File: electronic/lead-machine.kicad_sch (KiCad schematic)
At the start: 0 parts

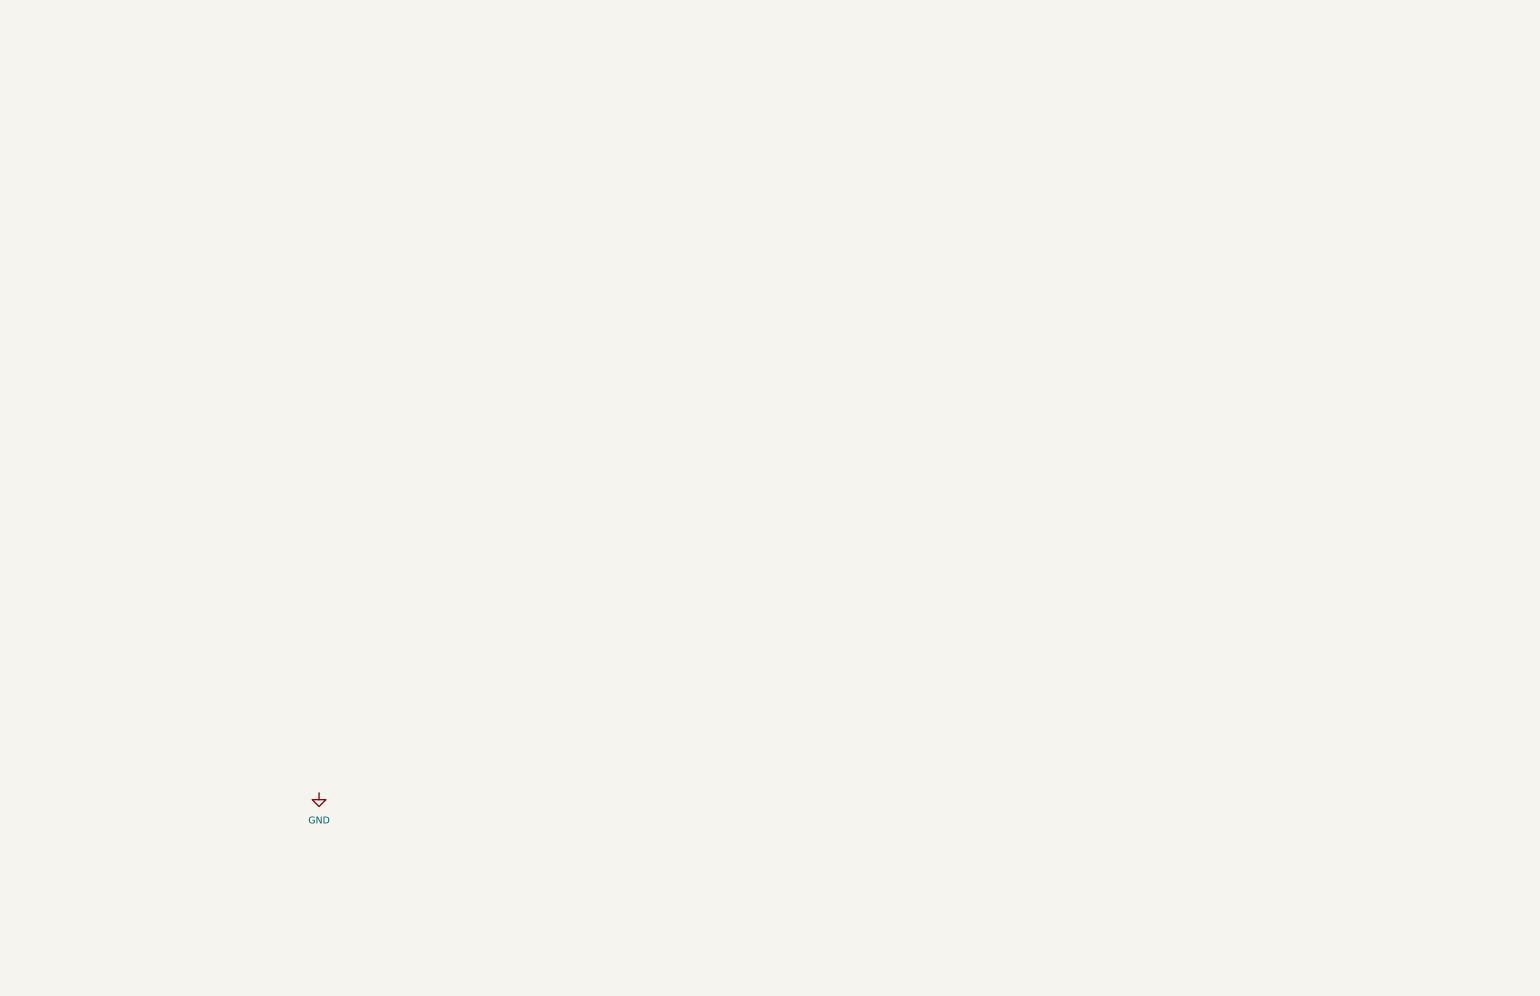
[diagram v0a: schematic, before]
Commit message: Add basic scheme for driver
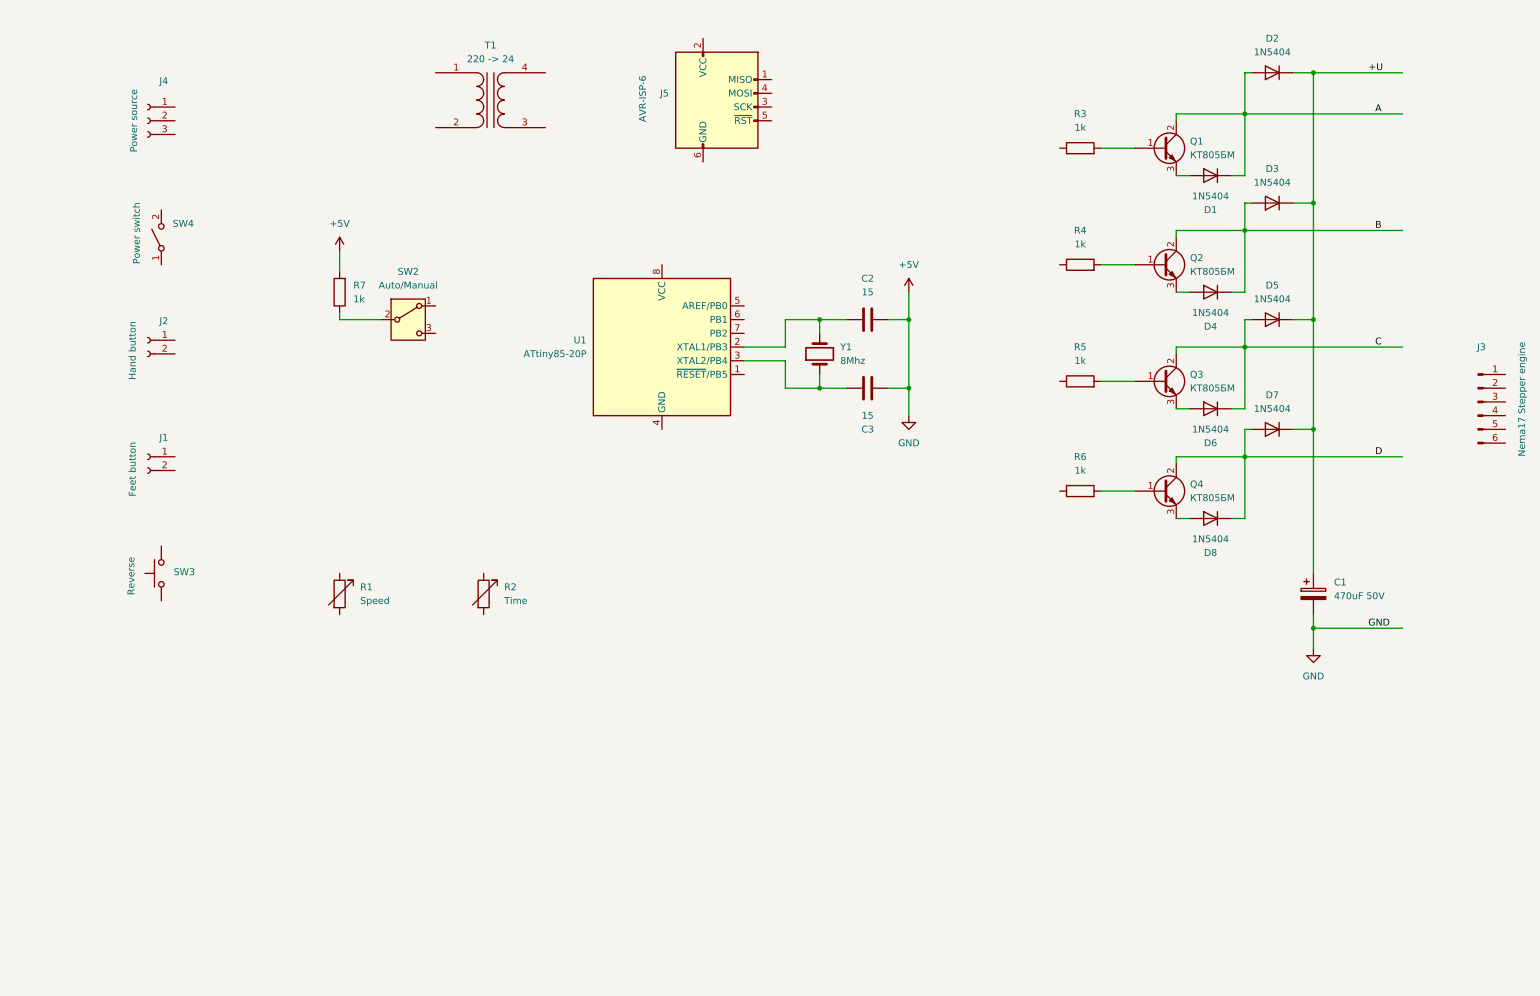
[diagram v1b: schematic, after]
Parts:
- added C1: 470uF 50V, symbol Device:C_Polarized
- added C2, C3: 15, symbol Device:C
- added D1, D2, D3, D4, D5, D6, D7, D8: 1N5404, Diode_THT:D_DO-201AD_P15.24mm_Horizontal, symbol Diode:1N5404
- added J1: Feet button, symbol Connector:Conn_01x02_Socket
- added J2: Hand button, symbol Connector:Conn_01x02_Socket
- added J3: Nema17 Stepper engine, Connector_Molex:Molex_KK-254_AE-6410-06A_1x06_P2.54mm_Vertical, symbol Connector:Conn_01x06_Pin
- added J4: Power source, symbol Connector:Conn_01x03_Socket
- added J5: AVR-ISP-6, symbol Connector:AVR-ISP-6
- added Q1, Q2, Q3, Q4: КТ805БМ, symbol Device:Q_NPN_BCE
- added R1: Speed, symbol Device:R_Variable
- added R2: Time, symbol Device:R_Variable
- added R3, R4, R5, R6, R7: 1k, symbol Device:R
- added SW2: Auto/Manual, symbol Switch:SW_SPDT
- added SW3: Reverse, symbol Switch:SW_Push
- added SW4: Power switch, symbol Switch:SW_SPST
- added T1: 220 -> 24, symbol Device:Transformer_1P_1S
- added U1: ATtiny85-20P, Package_DIP:DIP-8_W7.62mm, symbol MCU_Microchip_ATtiny:ATtiny85-20P
- added Y1: 8Mhz, symbol Device:Crystal
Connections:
- new net: D8.2 (A), Q4.3 (E)
- new net: C2.1, U1.2 (XTAL1/PB3), Y1.2
- new net: C3.1, U1.3 (XTAL2/PB4), Y1.1
- new net: Q4.1 (B), R6.2
- new net: Q2.1 (B), R4.2
- new net: D4.2 (A), Q2.3 (E)
- new net: D1.2 (A), Q1.3 (E)
- new net: D6.2 (A), Q3.3 (E)
- new net: R7.1, SW2.2 (B)
- new net: Q3.1 (B), R5.2
- new net: Q1.1 (B), R3.2
- new net +5V: C1.2, C2.2, C3.2, R7.2
- new net +U: C1.1, D2.1 (K), D3.1 (K), D5.1 (K), D7.1 (K)
- new net A: D1.1 (K), D2.2 (A), Q1.2 (C)
- new net B: D3.2 (A), D4.1 (K), Q2.2 (C)
- new net C: D5.2 (A), D6.1 (K), Q3.2 (C)
- new net D: D7.2 (A), D8.1 (K), Q4.2 (C)
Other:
- company: (none) -> SORC LLC
- title: (none) -> Lead machine controller

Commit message: Add bus line and button connections
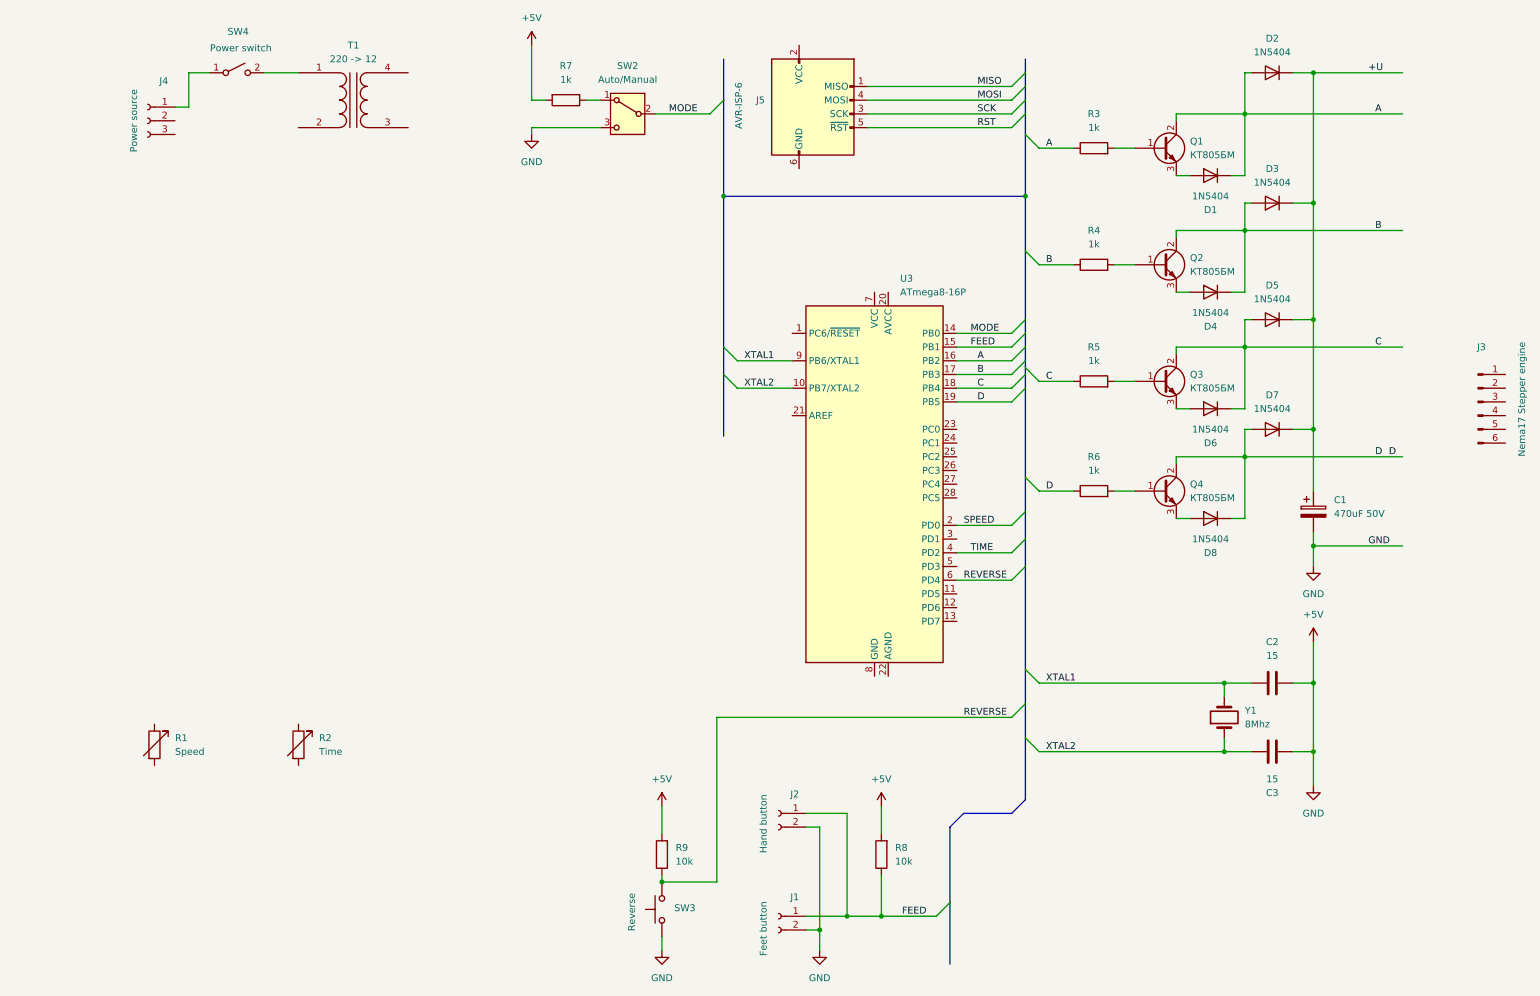
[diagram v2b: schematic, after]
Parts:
- removed U1: ATtiny85-20P, Package_DIP:DIP-8_W7.62mm, symbol MCU_Microchip_ATtiny:ATtiny85-20P
- added R8, R9: 10k, symbol Device:R
- added U3: ATmega8-16P, Package_DIP:DIP-28_W7.62mm, symbol MCU_Microchip_ATmega:ATmega8-16P
- T1: value 220 -> 24 -> 220 -> 12
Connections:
- net +5V: now also J1.2 (Pin_2), J2.2 (Pin_2), SW2.3 (C), SW3.1, R8.2, R9.2
- net A: now also R3.1, U3.16 (PB2)
- net B: now also R4.1, U3.17 (PB3)
- net C: now also R5.1, U3.18 (PB4)
- net D: now also R6.1, U3.19 (PB5)
- net XTAL1: now reaches C2.1, Y1.2
- net XTAL1: now also U3.9 (PB6/XTAL1)
- net XTAL2: now reaches C3.1, Y1.1
- net XTAL2: now also U3.10 (PB7/XTAL2)
- net at T1.1 (AA): now also SW4.2 (B)
- net REVERSE: now reaches SW3.2
- net REVERSE: now also R9.1, U3.6 (PD4)
- net at J4.1 (Pin_1): now also SW4.1 (A)
- net MISO: now reaches J5.1 (MISO)
- net SCK: now reaches J5.3 (SCK)
- net MOSI: now reaches J5.4 (MOSI)
- net RST: now reaches J5.5 (~{RST})
- net FEED: now reaches J1.1 (Pin_1)
- net FEED: now also J2.1 (Pin_1), R8.1, U3.15 (PB1)
- net at R7.1: now also SW2.1 (A); no longer SW2.2 (B)
- new net MODE: SW2.2 (B), U3.14 (PB0)
- new net SPEED: U3.2 (PD0)
- new net TIME: U3.4 (PD2)
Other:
- moved on the sheet: C1, C2, C3, J1, J2, J5, R1, R2, R3, R4, R5, R6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

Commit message: Add initial scheme connections
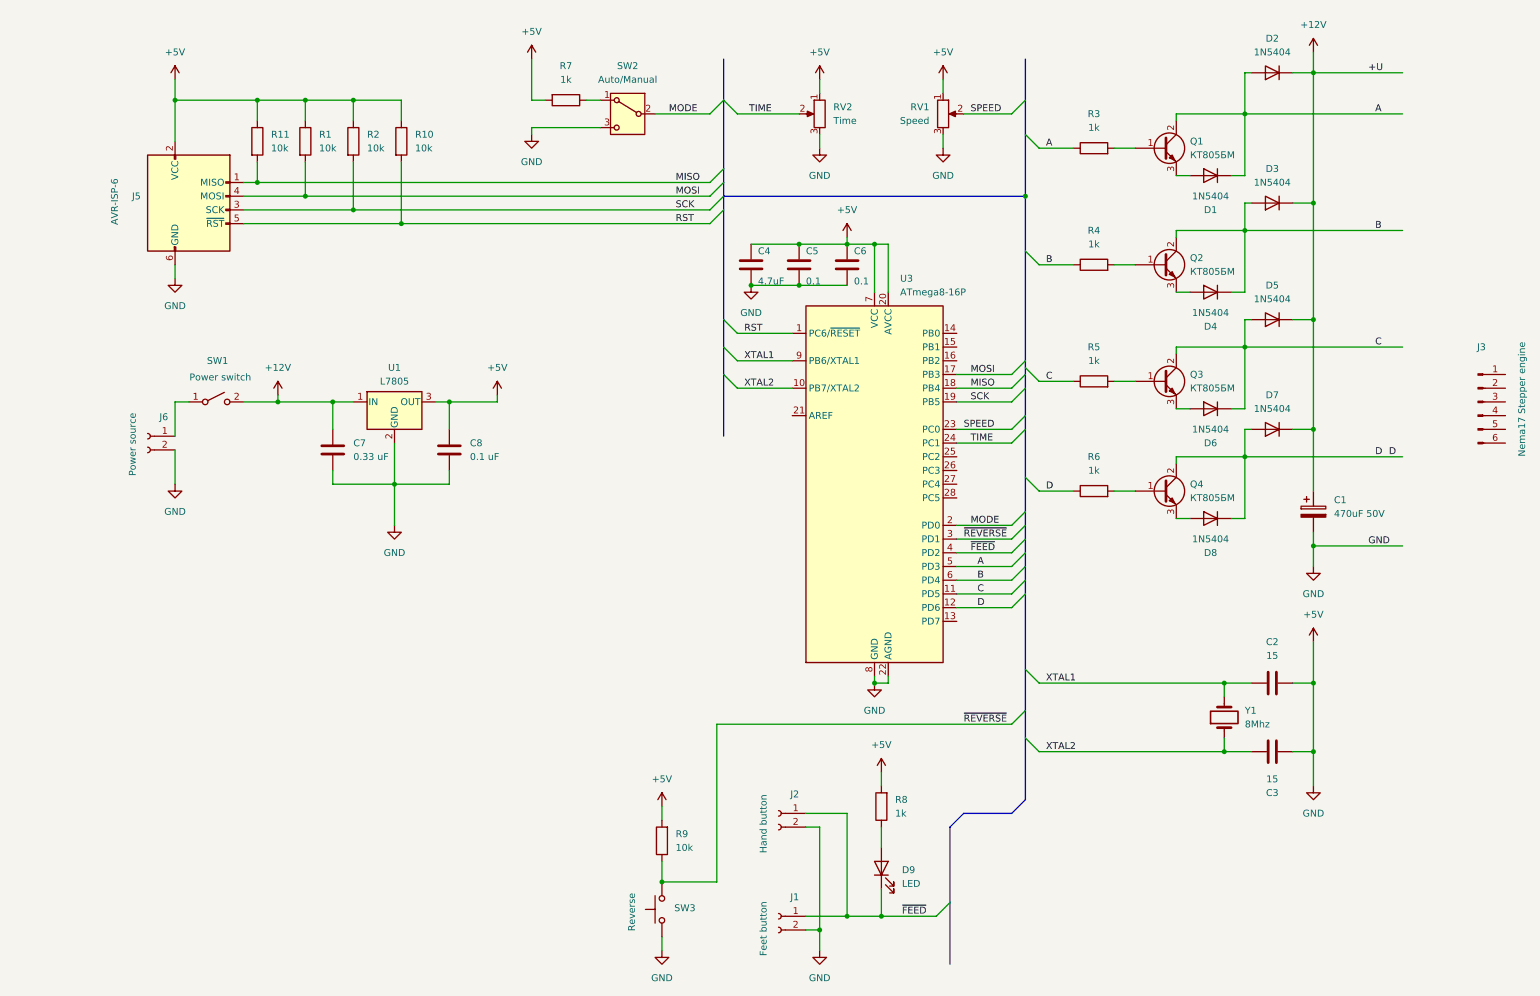
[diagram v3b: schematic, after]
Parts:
- removed J4: Power source, symbol Connector:Conn_01x03_Socket
- removed R1: Speed, symbol Device:R_Variable
- removed R2: Time, symbol Device:R_Variable
- removed SW4: Power switch, symbol Switch:SW_SPST
- removed T1: 220 -> 12, symbol Device:Transformer_1P_1S
- added C4: 4.7uF, symbol Device:C
- added C5, C6: 0.1, symbol Device:C
- added C7: 0.33 uF, Capacitor_SMD:C_1206_3216Metric_Pad1.33x1.80mm_HandSolder, symbol Device:C
- added C8: 0.1 uF, Capacitor_SMD:C_1206_3216Metric_Pad1.33x1.80mm_HandSolder, symbol Device:C
- added D9: LED, symbol Device:LED
- added J6: Power source, symbol Connector:Conn_01x02_Socket
- added R1, R10, R11, R2: 10k, symbol Device:R
- added RV1: Speed, symbol Device:R_Potentiometer
- added RV2: Time, symbol Device:R_Potentiometer
- added SW1: Power switch, symbol Switch:SW_SPST
- added U1: L7805, symbol Regulator_Linear:L7805
- R8: value 10k -> 1k
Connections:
- net +5V: now also J5.2 (VCC), J5.6 (GND), U3.20 (AVCC), U3.22 (AGND), U3.7 (VCC), U3.8 (GND), C4.1, C4.2, C5.1, C5.2, C6.1, C6.2, C7.2, C8.1, C8.2, J6.2 (Pin_2), R1.1, R10.1, R11.1, R2.1, RV1.1, RV1.3, RV2.1, RV2.3, U1.2 (GND), U1.3 (OUT)
- net A: now also U3.5 (PD3); no longer U3.16 (PB2)
- net B: now also U3.6 (PD4); no longer U3.17 (PB3)
- net C: now also U3.11 (PD5); no longer U3.18 (PB4)
- net D: now also U3.12 (PD6); no longer U3.19 (PB5)
- net MISO: now also U3.18 (PB4), R11.2
- net MODE: now also U3.2 (PD0); no longer U3.14 (PB0)
- net MOSI: now also U3.17 (PB3), R1.2
- net RST: now also U3.1 (PC6/~{RESET}), R10.2
- net SCK: now also U3.19 (PB5), R2.2
- net SPEED: now also U3.23 (PC0), RV1.2; no longer U3.2 (PD0)
- net TIME: now also U3.24 (PC1), RV2.2; no longer U3.4 (PD2)
- net ~{REVERSE}: now reaches U3.3 (PD1)
- net ~{REVERSE}: now also R9.1, SW3.2
- net +U renamed +12V
- net +12V: now also C7.1, SW1.2 (B), U1.1 (IN)
- net FEED renamed ~{FEED}
- net ~{FEED}: now also U3.4 (PD2), D9.1 (K); no longer R8.1, U3.15 (PB1)
- removed net REVERSE: R9.1, SW3.2, U3.6 (PD4)
- new net: J6.1 (Pin_1), SW1.1 (A)
- new net: D9.2 (A), R8.1
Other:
- moved on the sheet: R8, R9

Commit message: Add button code and machine initial class
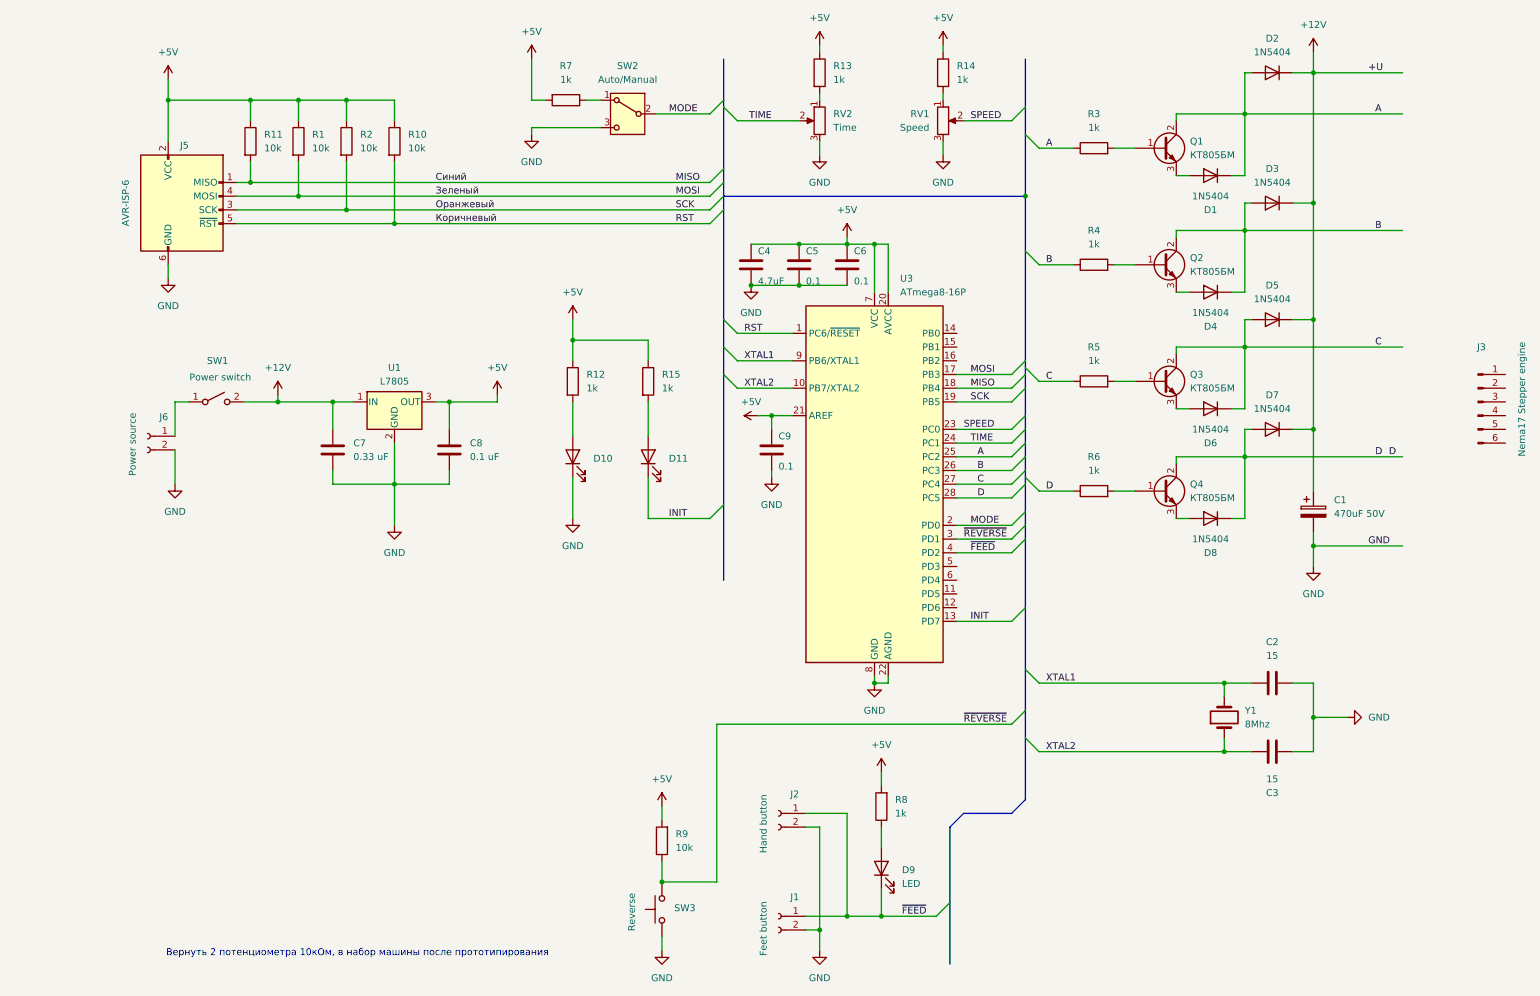
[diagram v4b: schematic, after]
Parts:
- added C9: 0.1, symbol Device:C
- added D10, D11: Green, LED_SMD:LED_1206_3216Metric_Pad1.42x1.75mm_HandSolder, symbol Device:LED
- added R12, R13, R14, R15: 1k, symbol Device:R
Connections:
- net +5V: now also U3.21 (AREF), C9.1, R12.1, R13.1, R14.1, R15.1; no longer C1.2, C2.2, C3.2, C4.2, C5.2, C6.2, C7.2, C8.2, J1.2 (Pin_2), J2.2 (Pin_2), J5.6 (GND), J6.2 (Pin_2), RV1.1, RV1.3, RV2.1, RV2.3, SW2.3 (C), SW3.1, U1.2 (GND), U3.22 (AGND), U3.8 (GND)
- net A: now also U3.25 (PC2); no longer U3.5 (PD3)
- net B: now also U3.26 (PC3); no longer U3.6 (PD4)
- net C: now also U3.27 (PC4); no longer U3.11 (PD5)
- net D: now also U3.28 (PC5); no longer U3.12 (PD6)
- net INIT: now reaches U3.13 (PD7)
- net INIT: now also D11.1 (K)
- new net: R13.2, RV2.1
- new net: R14.2, RV1.1
- new net: D10.2 (A), R12.2
- new net: D11.2 (A), R15.2
- new net GND: C1.2, C2.2, C3.2, C4.2, C5.2, C6.2, C7.2, C8.2, C9.2, D10.1 (K), J1.2 (Pin_2), J2.2 (Pin_2), J5.6 (GND), J6.2 (Pin_2), RV1.3, RV2.3, SW2.3 (C), SW3.1, U1.2 (GND), U3.22 (AGND), U3.8 (GND)
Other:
- note added: "Вернуть 2 потенциометра 10кОм, в набор машины после прототипирования"
- moved on the sheet: J5, R1, R10, R11, R2, RV1, RV2
